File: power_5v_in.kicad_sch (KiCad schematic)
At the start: 16 parts, among them U19 SY6280AAC, U3 LD1117V33

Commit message: WIP: Routed version, for first feedback round
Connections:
- net +3V3MCU renamed +3V3_MCU
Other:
- moved on the sheet: C15, C16, JP1, JP2, U3

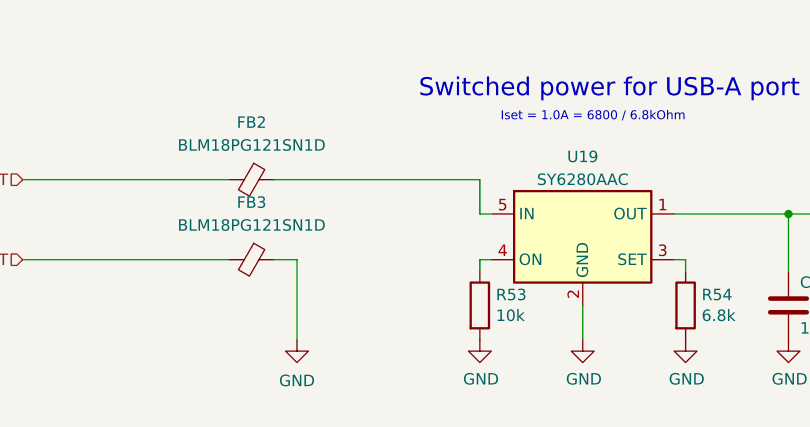
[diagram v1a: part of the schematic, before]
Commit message: Labeled expansion port, fixed en pin U19 (high)
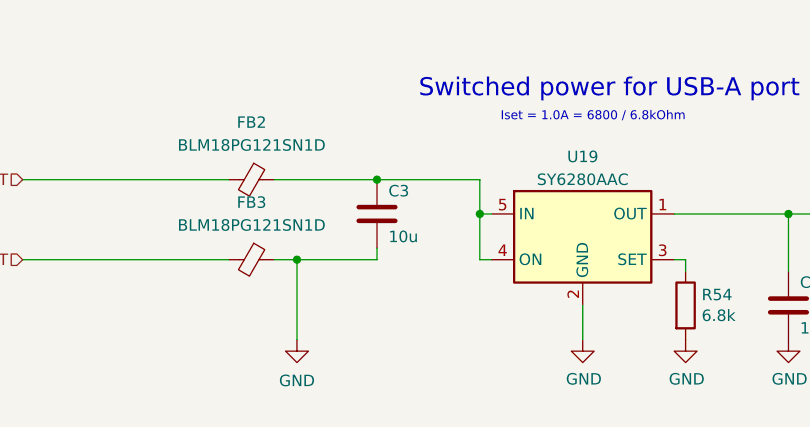
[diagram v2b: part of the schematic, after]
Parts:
- removed R53: 10k, Resistor_SMD:R_0402_1005Metric, symbol mch2021-rescue:R-Device
- added C3: 10u, Capacitor_SMD:C_0805_2012Metric, symbol Device:C
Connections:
- net GND: now also C3.2
- net at U19.4 (ON): now also FB2.1, U19.5 (IN), C3.1
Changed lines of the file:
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@@
+	)
+	(junction
+		(at 80.01 80.01)
+		(diameter 0)
+		(color 0 0 0 0)
 	)
 	(junction
@@
 	)
 	(junction
+		(at 59.69 85.09)
+		(diameter 0)
+		(color 0 0 0 0)
+	)
+	(junction
 		(at 140.97 80.01)
 		(diameter 0)
 		(color 0 0 0 0)
 	)
+	(junction
+		(at 68.58 76.2)
+		(diameter 0)
+		(color 0 0 0 0)
+	)
 	(wire
 		(pts
@@
 	(wire
 		(pts
-			(xy 57.15 76.2) (xy 80.01 76.2)
+			(xy 57.15 76.2) (xy 68.58 76.2)
+		)
+		(stroke
+			(width 0)
+			(type default)
+		)
+	)
+	(wire
+		(pts
+			(xy 68.58 83.82) (xy 68.58 85.09)
 		)
 		(stroke
@@
 	(wire
 		(pts
+			(xy 59.69 85.09) (xy 68.58 85.09)
+		)
+		(stroke
+			(width 0)
+			(type default)
+		)
+	)
+	(wire
+		(pts
 			(xy 41.91 19.05) (xy 54.61 19.05)
 		)
@@
 	(wire
 		(pts
+			(xy 68.58 76.2) (xy 80.01 76.2)
+		)
+		(stroke
+			(width 0)
+			(type default)
+		)
+	)
+	(wire
+		(pts
 			(xy 29.21 76.2) (xy 52.07 76.2)
 		)
@@
 	(wire
 		(pts
-			(xy 80.01 85.09) (xy 80.01 86.36)
-		)
-		(stroke
-			(width 0)
-			(type default)
-		)
-	)
-	(wire
-		(pts
 			(xy 80.01 76.2) (xy 80.01 80.01)
+		)
+		(stroke
+			(width 0)
+			(type default)
+		)
+	)
+	(wire
+		(pts
+			(xy 80.01 80.01) (xy 80.01 85.09)
 		)
 		(stroke
@@
 	)
 	(symbol
-		(lib_id "mch2021-rescue:R-Device")
-		(at 80.01 90.17 0)
-		(unit 1)
-		(exclude_from_sim no)
-		(in_bom yes)
-		(on_board yes)
-		(dnp no)
-		(property "Reference" "R53"
-			(at 81.788 89.0016 0)
-			(effects
-				(font
-					(size 1.27 1.27)
-				)
-				(justify left)
-			)
-		)
-		(property "Value" "10k"
-			(at 81.788 91.313 0)
-			(effects
-				(font
-					(size 1.27 1.27)
-				)
-				(justify left)
-			)
-		)
-		(property "Footprint" "Resistor_SMD:R_0402_1005Metric"
-			(at 78.232 90.17 90)
-			(effects
-				(font
-					(size 1.27 1.27)
-				)
-				(hide yes)
-			)
-		)
-		(property "Datasheet" "https://datasheet.lcsc.com/lcsc/2304140030_YAGEO-RC0402FR-0710KL_C60490.pdf"
-			(at 80.01 90.17 0)
-			(effects
-				(font
-					(size 1.27 1.27)
-				)
-				(hide yes)
-			)
-		)
-		(property "Description" ""
-			(at 80.01 90.17 0)
-			(effects
-				(font
-					(size 1.27 1.27)
-				)
-				(hide yes)
-			)
-		)
-		(property "LCSC" "C60490"
-			(at 80.01 90.17 0)
-			(effects
-				(font
-					(size 1.27 1.27)
-				)
-				(hide yes)
-			)
-		)
-		(property "MANUFACTURER" ""
-			(at 80.01 90.17 0)
-			(effects
-				(font
-					(size 1.27 1.27)
-				)
-				(hide yes)
-			)
-		)
-		(property "Check_prices" ""
-			(at 80.01 90.17 0)
-			(effects
-				(font
-					(size 1.27 1.27)
-				)
-				(hide yes)
-			)
-		)
-		(property "Description_1" ""
-			(at 80.01 90.17 0)
-			(effects
-				(font
-					(size 1.27 1.27)
-				)
-				(hide yes)
-			)
-		)
-		(property "Category" ""
-			(at 80.01 90.17 0)
-			(effects
-				(font
-					(size 1.27 1.27)
-				)
-				(hide yes)
-			)
-		)
-		(pin "1"
-		)
-		(pin "2"
-		)
-		(instances
-			(project "stopnu-hardware"
-				(path "/4ab90003-ea4c-4878-8117-f834ac24f8d9/9fd6a918-45bc-4af1-b3e2-71cdbd26c0f6"
-					(reference "R53")
-					(unit 1)
-				)
-			)
-		)
-	)
-	(symbol
 		(lib_id "Device:C_Small")
 		(at 41.91 21.59 0)
@@
 	)
 	(symbol
-		(lib_id "mch2021-rescue:GND-power")
-		(at 80.01 93.98 0)
-		(unit 1)
-		(exclude_from_sim no)
-		(in_bom yes)
-		(on_board yes)
-		(dnp no)
-		(property "Reference" "#PWR0205"
-			(at 80.01 100.33 0)
-			(effects
-				(font
-					(size 1.27 1.27)
-				)
-				(hide yes)
-			)
-		)
-		(property "Value" "GND"
-			(at 80.137 98.3742 0)
-			(effects
-				(font
-					(size 1.27 1.27)
-				)
-			)
-		)
-		(property "Footprint" ""
-			(at 80.01 93.98 0)
-			(effects
-				(font
-					(size 1.27 1.27)
-				)
-				(hide yes)
-			)
-		)
-		(property "Datasheet" ""
-			(at 80.01 93.98 0)
-			(effects
-				(font
-					(size 1.27 1.27)
-				)
-				(hide yes)
-			)
-		)
-		(property "Description" ""
-			(at 80.01 93.98 0)
-			(effects
-				(font
-					(size 1.27 1.27)
-				)
-				(hide yes)
-			)
-		)
-		(pin "1"
-		)
-		(instances
-			(project "stopnu-hardware"
-				(path "/4ab90003-ea4c-4878-8117-f834ac24f8d9/9fd6a918-45bc-4af1-b3e2-71cdbd26c0f6"
-					(reference "#PWR0205")
-					(unit 1)
-				)
-			)
-		)
-	)
-	(symbol
 		(lib_id "Device:FerriteBead_Small")
 		(at 54.61 76.2 270)
@@
 					(unit 1)
 				)
+			)
+		)
+	)
+	(symbol
+		(lib_id "Device:C")
+		(at 68.58 80.01 0)
+		(unit 1)
+		(exclude_from_sim no)
+		(in_bom yes)
+		(on_board yes)
+		(dnp no)
+		(property "Reference" "C3"
+			(at 69.85 77.47 0)
+			(effects
+				(font
+					(size 1.27 1.27)
+				)
+				(justify left)
+			)
+		)
+		(property "Value" "10u"
+			(at 69.85 82.55 0)
+			(effects
+				(font
+					(size 1.27 1.27)
+				)
+				(justify left)
+			)
+		)
+		(property "Footprint" "Capacitor_SMD:C_0805_2012Metric"
+			(at 69.5452 83.82 0)
+			(effects
+				(font
+					(size 1.27 1.27)
+				)
+				(hide yes)
+			)
+		)
+		(property "Datasheet" "https://www.lcsc.com/product-detail/Multilayer-Ceramic-Capacitors-MLCC-SMD-SMT_Samsung-Electro-Mechanics-CL21B106KAYQNNE_C3039694.html"
+			(at 68.58 80.01 0)
+			(effects
+				(font
+					(size 1.27 1.27)
+				)
+				(hide yes)
+			)
+		)
+		(property "Description" ""
+			(at 68.58 80.01 0)
+			(effects
+				(font
+					(size 1.27 1.27)
+				)
+				(hide yes)
+			)
+		)
+		(property "LCSC" "C3039694"
+			(at 68.58 80.01 0)
+			(effects
+				(font
+					(size 1.27 1.27)
+				)
+				(hide yes)
+			)
+		)
+		(property "Check_prices" ""
+			(at 68.58 80.01 0)
+			(effects
+				(font
+					(size 1.27 1.27)
+				)
+				(hide yes)
+			)
+		)
+		(property "Description_1" ""
+			(at 68.58 80.01 0)
+			(effects
+				(font
+					(size 1.27 1.27)
+				)
+				(hide yes)
+			)
+		)
+		(property "Category" ""
+			(at 68.58 80.01 0)
+			(effects
+				(font
+					(size 1.27 1.27)
+				)
+				(hide yes)
+			)
+		)
+		(pin "1"
+		)
+		(pin "2"
+		)
+		(instances
+			(project "stopnu-hardware"
+				(path "/4ab90003-ea4c-4878-8117-f834ac24f8d9/9fd6a918-45bc-4af1-b3e2-71cdbd26c0f6"
+					(reference "C3")
+					(unit 1)
+				)

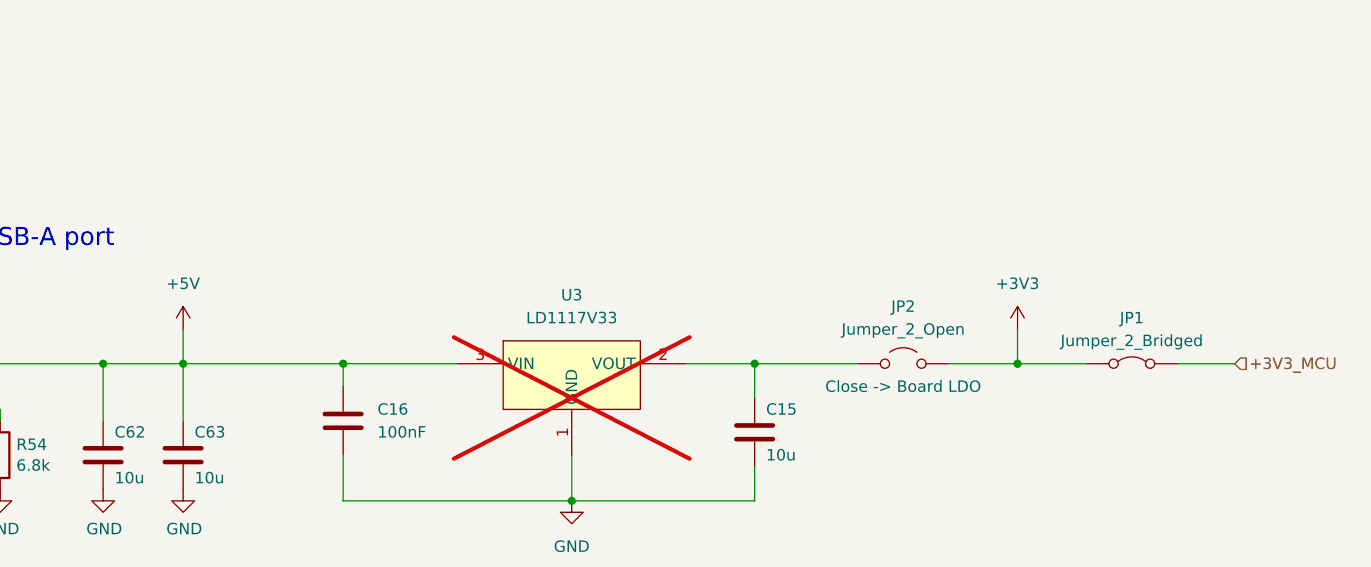
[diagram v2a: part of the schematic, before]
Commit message: Add README.md, make power input more intuitive in schematic.
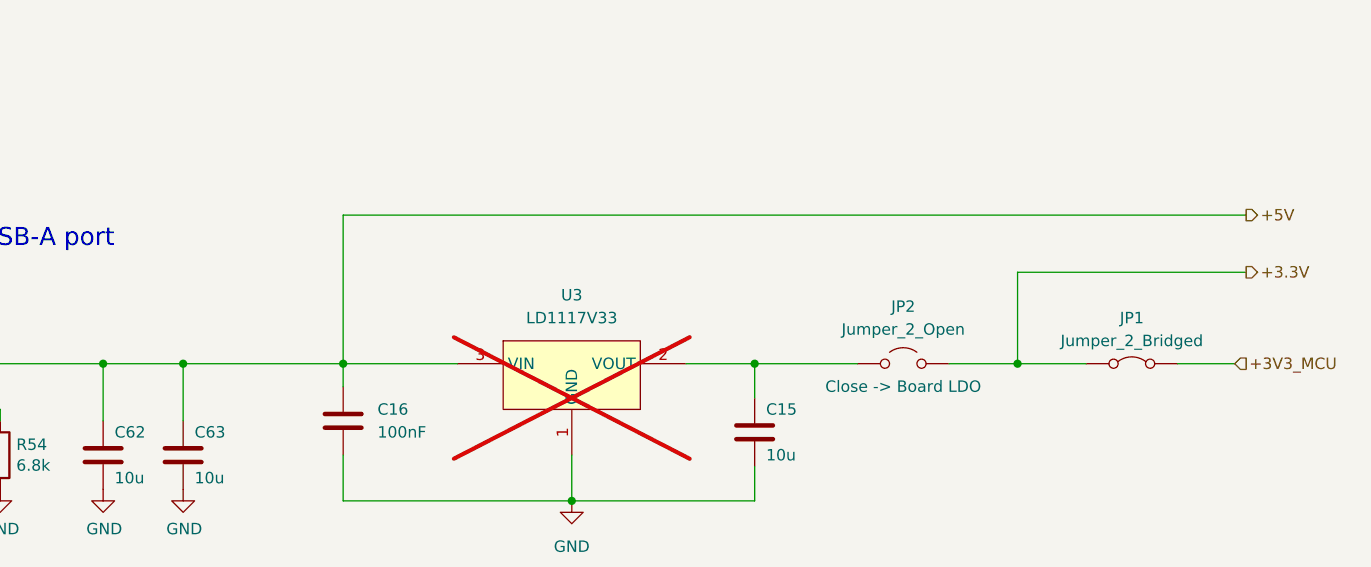
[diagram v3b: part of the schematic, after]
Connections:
- net +3V3: no longer JP1.1 (A), JP2.2 (B)
- new net +3.3V: JP1.1 (A), JP2.2 (B)
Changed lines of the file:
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@@
+	(wire
+		(pts
+			(xy 215.9 69.85) (xy 241.3 69.85)
+		)
+		(stroke
+			(width 0)
+			(type default)
+		)
+	)
 	(wire
 		(pts
@@
 	(wire
 		(pts
-			(xy 215.9 76.2) (xy 215.9 80.01)
-		)
-		(stroke
-			(width 0)
-			(type default)
-		)
-	)
-	(wire
-		(pts
 			(xy 140.97 95.25) (xy 166.37 95.25)
 		)
@@
 	(wire
 		(pts
+			(xy 140.97 63.5) (xy 241.3 63.5)
+		)
+		(stroke
+			(width 0)
+			(type default)
+		)
+	)
+	(wire
+		(pts
+			(xy 140.97 63.5) (xy 140.97 80.01)
+		)
+		(stroke
+			(width 0)
+			(type default)
+		)
+	)
+	(wire
+		(pts
 			(xy 208.28 80.01) (xy 215.9 80.01)
 		)
@@
 	(wire
 		(pts
-			(xy 123.19 76.2) (xy 123.19 80.01)
-		)
-		(stroke
-			(width 0)
-			(type default)
-		)
-	)
-	(wire
-		(pts
 			(xy 54.61 19.05) (xy 60.96 19.05)
 		)
@@
 		(pts
 			(xy 123.19 80.01) (xy 123.19 86.36)
+		)
+		(stroke
+			(width 0)
+			(type default)
+		)
+	)
+	(wire
+		(pts
+			(xy 215.9 69.85) (xy 215.9 80.01)
 		)
 		(stroke
@@
 		)
 	)
+	(hierarchical_label "+3.3V"
+		(shape output)
+		(at 241.3 69.85 0)
+		(effects
+			(font
+				(size 1.27 1.27)
+			)
+			(justify left)
+		)
+	)
 	(hierarchical_label "+3V3_MCU"
 		(shape input)
 		(at 240.03 80.01 0)
+		(effects
+			(font
+				(size 1.27 1.27)
+			)
+			(justify left)
+		)
+	)
+	(hierarchical_label "+5V"
+		(shape output)
+		(at 241.3 63.5 0)
 		(effects
 			(font
@@
 	)
 	(symbol
-		(lib_id "power:+3V3")
-		(at 215.9 76.2 0)
-		(unit 1)
-		(exclude_from_sim no)
-		(in_bom yes)
-		(on_board yes)
-		(dnp no)
-		(fields_autoplaced yes)
-		(property "Reference" "#PWR041"
-			(at 215.9 80.01 0)
-			(effects
-				(font
-					(size 1.27 1.27)
-				)
-				(hide yes)
-			)
-		)
-		(property "Value" "+3V3"
-			(at 215.9 71.12 0)
-			(effects
-				(font
-					(size 1.27 1.27)
-				)
-			)
-		)
-		(property "Footprint" ""
-			(at 215.9 76.2 0)
-			(effects
-				(font
-					(size 1.27 1.27)
-				)
-				(hide yes)
-			)
-		)
-		(property "Datasheet" ""
-			(at 215.9 76.2 0)
-			(effects
-				(font
-					(size 1.27 1.27)
-				)
-				(hide yes)
-			)
-		)
-		(property "Description" "Power symbol creates a global label with name \"+3V3\""
-			(at 215.9 76.2 0)
-			(effects
-				(font
-					(size 1.27 1.27)
-				)
-				(hide yes)
-			)
-		)
-		(pin "1"
-		)
-		(instances
-			(project ""
-				(path "/4ab90003-ea4c-4878-8117-f834ac24f8d9/9fd6a918-45bc-4af1-b3e2-71cdbd26c0f6"
-					(reference "#PWR041")
-					(unit 1)
-				)
-			)
-		)
-	)
-	(symbol
 		(lib_id "mch2021-rescue:GND-power")
 		(at 91.44 93.98 0)
@@
 					(unit 1)
 				)
-			)
-		)
-	)
-	(symbol
-		(lib_id "power:+5V")
-		(at 123.19 76.2 0)
-		(unit 1)
-		(exclude_from_sim no)
-		(in_bom yes)
-		(on_board yes)
-		(dnp no)
-		(fields_autoplaced yes)
-		(property "Reference" "#PWR036"
-			(at 123.19 80.01 0)
-			(effects
-				(font
-					(size 1.27 1.27)
-				)
-				(hide yes)
-			)
-		)
-		(property "Value" "+5V"
-			(at 123.19 71.12 0)
-			(effects
-				(font
-					(size 1.27 1.27)
-				)
-			)
-		)
-		(property "Footprint" ""
-			(at 123.19 76.2 0)
-			(effects
-				(font
-					(size 1.27 1.27)
-				)
-				(hide yes)
-			)
-		)
-		(property "Datasheet" ""
-			(at 123.19 76.2 0)
-			(effects
-				(font
-					(size 1.27 1.27)
-				)
-				(hide yes)
-			)
-		)
-		(property "Description" "Power symbol creates a global label with name \"+5V\""
-			(at 123.19 76.2 0)
-			(effects
-				(font
-					(size 1.27 1.27)
-				)
-				(hide yes)
-			)
-		)
-		(pin "1"
-		)
-		(instances
-			(project ""
-				(path "/4ab90003-ea4c-4878-8117-f834ac24f8d9/9fd6a918-45bc-4af1-b3e2-71cdbd26c0f6"
-					(reference "#PWR036")
-					(unit 1)
-				)

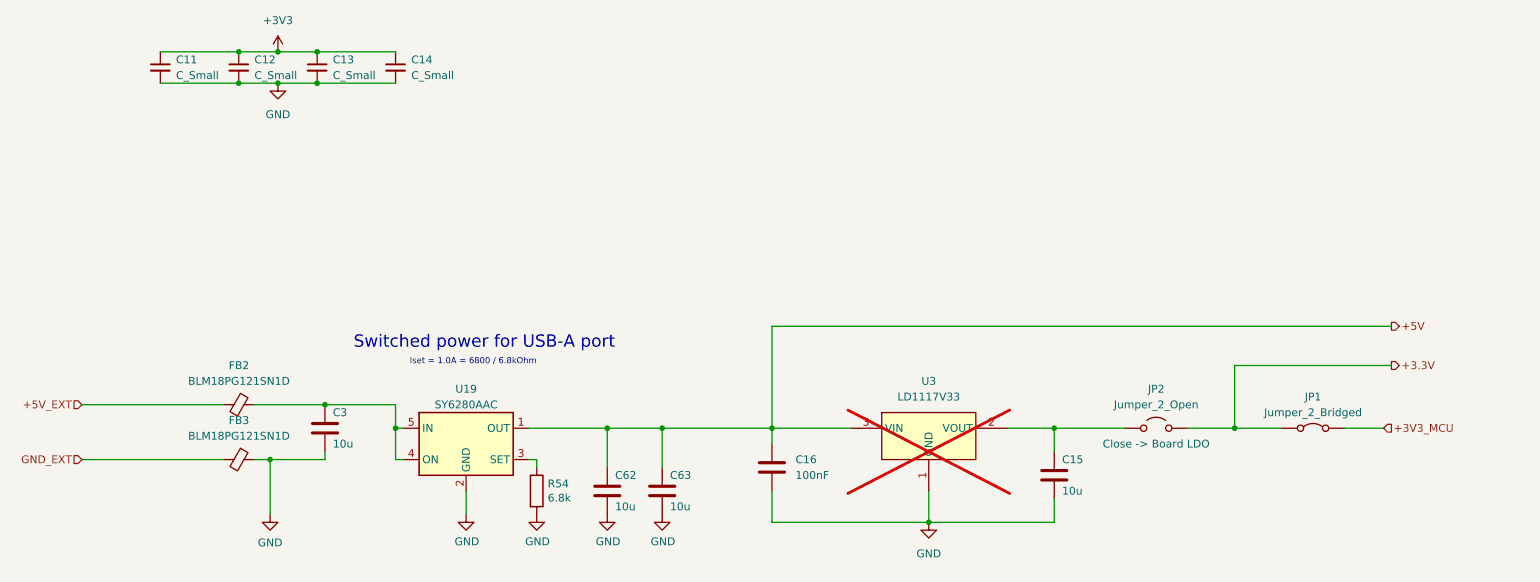
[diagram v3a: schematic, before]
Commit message: Fixed issues + added 3 2 pin connectors for digital (button) inputs.
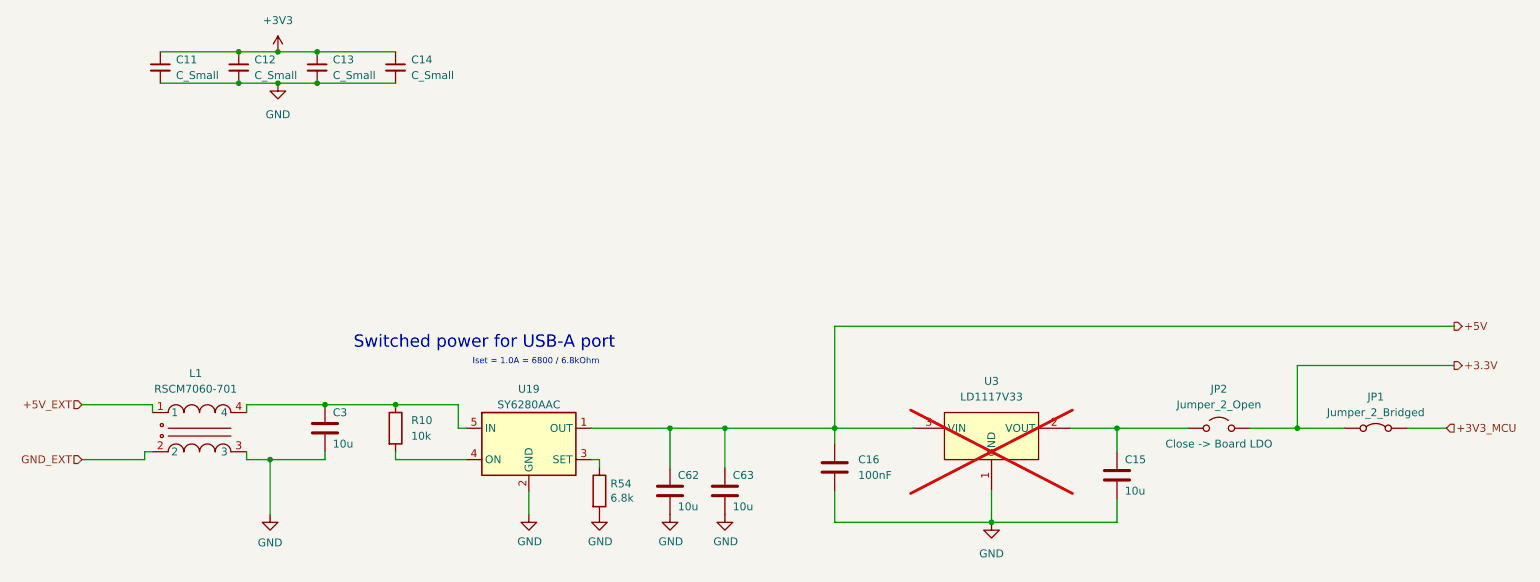
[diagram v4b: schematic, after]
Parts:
- removed FB2, FB3: BLM18PG121SN1D, Inductor_SMD:L_0603_1608Metric, symbol Device:FerriteBead_Small
- added L1: RSCM7060-701, lcsc:FILTER-SMD_4P-L7.0-W6.0-P3.00-TL, symbol lcsc:RSCM7060-701
- added R10: 10k, Resistor_SMD:R_0603_1608Metric, symbol Device:R
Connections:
- net +5V_EXT: now also L1.1
- net GND: now also L1.3
- net GND_EXT: now also L1.2
- net at C3.1, U19.5 (IN): now also L1.4, R10.1; no longer U19.4 (ON)
- new net: R10.2, U19.4 (ON)
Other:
- moved on the sheet: C15, C16, C62, C63, JP1, JP2, R54, U19, U3

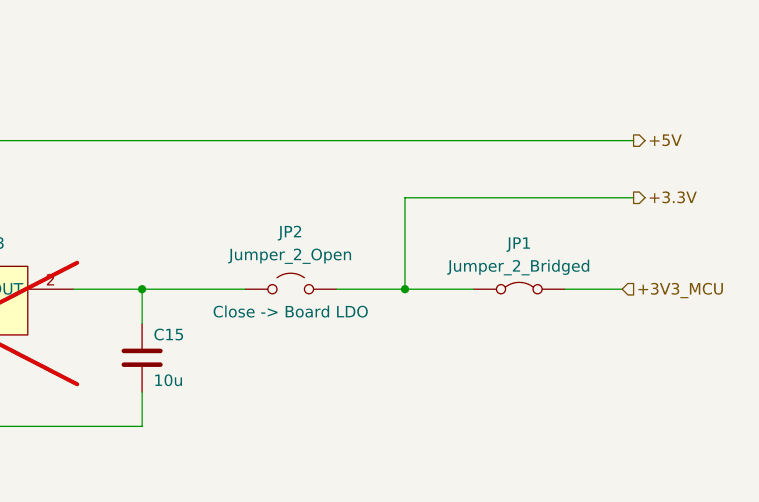
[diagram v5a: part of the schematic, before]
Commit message: Fixed fabrication files, so PCBA will work with the correct rotation of the components.
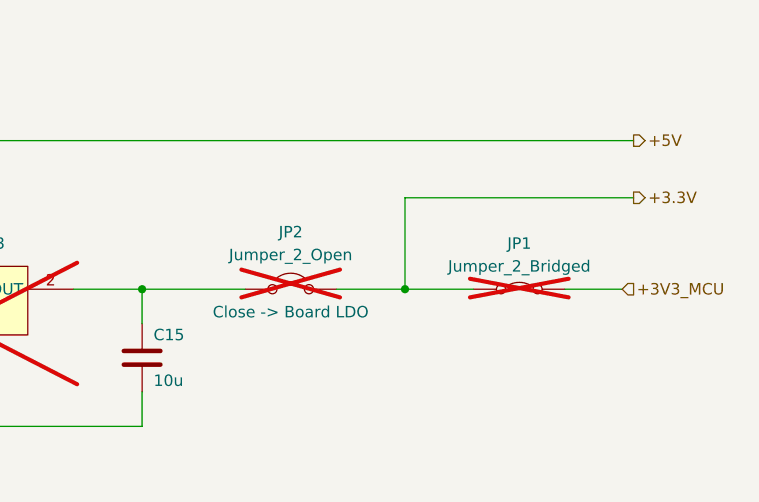
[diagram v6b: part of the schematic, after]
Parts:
- C16: LCSC C14663 -> C49678
- JP1, JP2: now not fitted; now left out of the parts list
- U19: Rotation Offset (none) -> 90
- U3: now left out of the parts list
